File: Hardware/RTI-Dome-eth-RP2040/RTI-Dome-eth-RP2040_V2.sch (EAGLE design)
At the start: 104 parts, among them IC2 24LC128T-I_SN, IC3 FT232RL, IC4 RASPBERRY_PI_PICO, IC8 REG1117-3.3V, IC9 REG1117-5V, J2 XT60PW-M, U1 W5500, X13 PN61729-S, X9 J1011F21PNL

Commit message: Added transistor for stepper controller output
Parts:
- added R12, R22, R41: 1K, rcl:R-EU_R0805
- added T1, T2, T3: (no value), transistor:MMBT3904LT1-NPN-SOT23-BEC
- IC2: value 24LC128T-I_SN -> 24LC64T-I/SN; device rti:24LC128T-I_SN -> Microchip_By_element14_Batch_1:24LC64T-I/SN
- R13, R14, R19: value 1K -> 10K
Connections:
- removed net AT_PARK_PIN_LOOP: U$1G$1.A3
- removed net AT_PARK_PIN_LOOP_EXT: U$1G$1.Y3
- new net DIR-5V_PULLUP: R13.1, R22.1, T2.B
- new net DIR_5V_OUT: T2.E, X10-2.KL
- new net EN-5V_PULLUP: R12.1, R14.2, T1.B
- new net EN_5V_OUT: T1.E, X2-2.KL
- new net STEP-5V_PULLUP: R19.2, R41.1, T3.B
- new net STEP_5V_OUT: T3.E, X6-2.KL
- net BUTTON_EAST_OPEN-IN_EXT: no longer R44.2
- net BUTTON_WEST_CLOSE-IN_EXT: no longer R47.2
- net GND: now also U$1G$1.A3
- net HOME_SHUTTER_CLOSED-IN_EXT: no longer R50.2
- net M_DIR_5V: now also R22.2; no longer R19.2, X10-2.KL
- net M_EN_5V: now also R12.2; no longer R14.2, X2-2.KL
- net M_STEP_5V: now also R41.2; no longer R13.1, X6-2.KL
- net RG-11-IN_EXT: no longer R5.2
- net SHUTTER_OPENED-IN_EXT: no longer R48.2
- net VCC: now also T1.C, T2.C
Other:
- moved on the sheet: C23, C24, C27, C28, C4, C40, C41, C42, C43, C45, C5, C6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

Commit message: Fix some issue after the schematics snap to grid.
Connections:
- net BUTTON_EAST_OPEN-IN_EXT: now also R44.2
- net BUTTON_WEST_CLOSE-IN_EXT: now also R47.2
- net HOME_SHUTTER_CLOSED-IN_EXT: now also R50.2
- net RG-11-IN_EXT: now also R5.2
- net SHUTTER_OPENED-IN_EXT: now also R48.2
- net VCC: now also T3.C
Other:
- moved on the sheet: C1, C40, C41, C42, C43, C44, C45, C46, C8, IC3, IC4, R11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

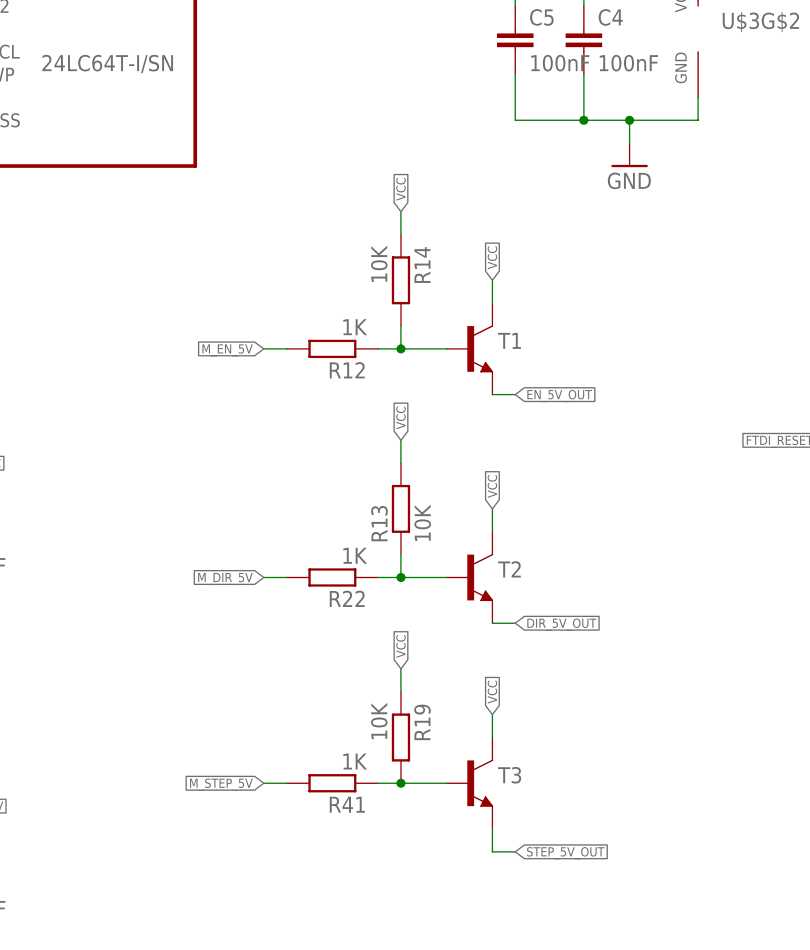
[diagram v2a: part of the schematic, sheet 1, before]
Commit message: Remove unused pull-up
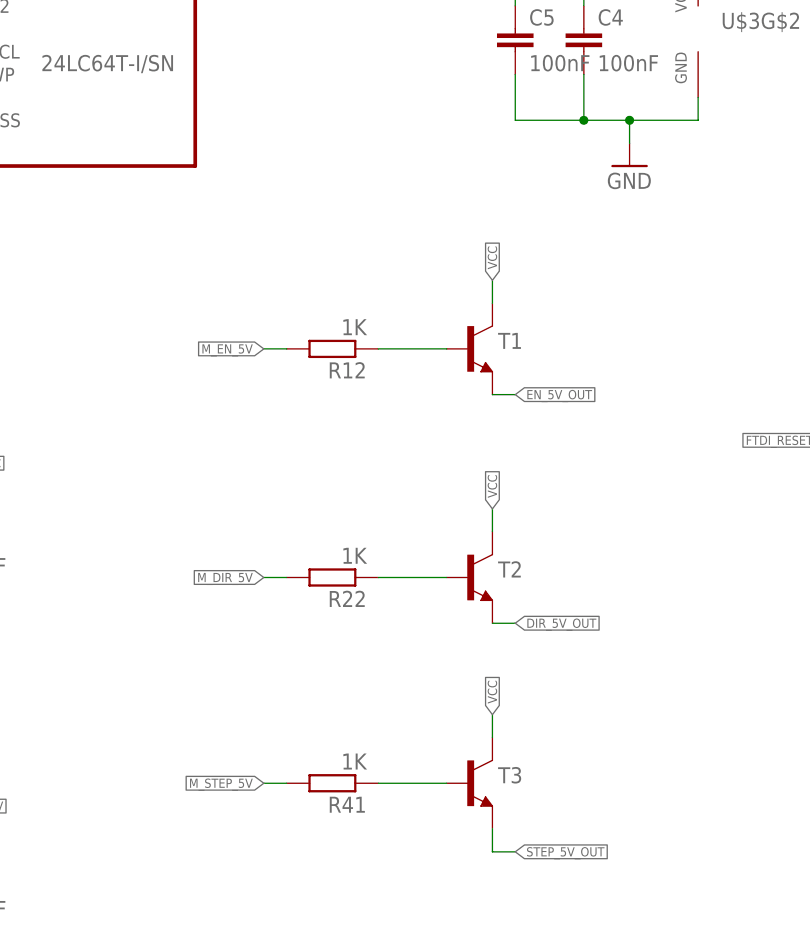
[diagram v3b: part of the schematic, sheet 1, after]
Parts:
- removed R13, R14, R19: 10K, rcl:R-EU_R0805
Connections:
- removed net DIR-5V_PULLUP: R13.1, R22.1, T2.B
- removed net EN-5V_PULLUP: R12.1, R14.2, T1.B
- removed net STEP-5V_PULLUP: R19.2, R41.1, T3.B
- new net DIR-5V_TR: R22.1, T2.B
- new net EN-5V_TR: R12.1, T1.B
- new net STEP-5V_TR: R41.1, T3.B
- net VCC: no longer R13.2, R14.1, R19.1
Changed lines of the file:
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@@
 <part name="GND4" library="supply1" library_urn="urn:adsk.eagle:library:371" deviceset="GND" device=""/>
 <part name="P+4" library="supply1" library_urn="urn:adsk.eagle:library:371" deviceset="VCC" device=""/>
-<part name="R13" library="rcl" library_urn="urn:adsk.eagle:library:334" deviceset="R-EU_" device="R0805" package3d_urn="urn:adsk.eagle:package:23553/2" value="10K">
+<part name="R15" library="rcl" library_urn="urn:adsk.eagle:library:334" deviceset="R-EU_" device="R0805" package3d_urn="urn:adsk.eagle:package:23553/2" value="4.7K">
 <spice>
 <pinmapping spiceprefix="R">
@@
 <attribute name="MPN" value="RT0805FRE074K7L"/>
 </part>
-<part name="R14" library="rcl" library_urn="urn:adsk.eagle:library:334" deviceset="R-EU_" device="R0805" package3d_urn="urn:adsk.eagle:package:23553/2" value="10K">
+<part name="R16" library="rcl" library_urn="urn:adsk.eagle:library:334" deviceset="R-EU_" device="R0805" package3d_urn="urn:adsk.eagle:package:23553/2" value="4.7K">
 <spice>
 <pinmapping spiceprefix="R">
@@
 <attribute name="MPN" value="RT0805FRE074K7L"/>
 </part>
-<part name="R15" library="rcl" library_urn="urn:adsk.eagle:library:334" deviceset="R-EU_" device="R0805" package3d_urn="urn:adsk.eagle:package:23553/2" value="4.7K">
+<part name="R17" library="rcl" library_urn="urn:adsk.eagle:library:334" deviceset="R-EU_" device="R0805" package3d_urn="urn:adsk.eagle:package:23553/2" value="4.7K">
 <spice>
 <pinmapping spiceprefix="R">
@@
 <attribute name="MPN" value="RT0805FRE074K7L"/>
 </part>
-<part name="R16" library="rcl" library_urn="urn:adsk.eagle:library:334" deviceset="R-EU_" device="R0805" package3d_urn="urn:adsk.eagle:package:23553/2" value="4.7K">
-<spice>
-<pinmapping spiceprefix="R">
-<pinmap gate="G$1" pin="1" pinorder="1"/>
-<pinmap gate="G$1" pin="2" pinorder="2"/>
-</pinmapping>
-</spice>
-<attribute name="MPN" value="RT0805FRE074K7L"/>
-</part>
-<part name="R17" library="rcl" library_urn="urn:adsk.eagle:library:334" deviceset="R-EU_" device="R0805" package3d_urn="urn:adsk.eagle:package:23553/2" value="4.7K">
-<spice>
-<pinmapping spiceprefix="R">
-<pinmap gate="G$1" pin="1" pinorder="1"/>
-<pinmap gate="G$1" pin="2" pinorder="2"/>
-</pinmapping>
-</spice>
-<attribute name="MPN" value="RT0805FRE074K7L"/>
-</part>
 <part name="R18" library="rcl" library_urn="urn:adsk.eagle:library:334" deviceset="R-EU_" device="R0805" package3d_urn="urn:adsk.eagle:package:23553/2" value="4.7K">
-<spice>
-<pinmapping spiceprefix="R">
-<pinmap gate="G$1" pin="1" pinorder="1"/>
-<pinmap gate="G$1" pin="2" pinorder="2"/>
-</pinmapping>
-</spice>
-<attribute name="MPN" value="RT0805FRE074K7L"/>
-</part>
-<part name="R19" library="rcl" library_urn="urn:adsk.eagle:library:334" deviceset="R-EU_" device="R0805" package3d_urn="urn:adsk.eagle:package:23553/2" value="10K">
 <spice>
 <pinmapping spiceprefix="R">
@@
 <attribute name="VALUE" x="306.07" y="254" size="1.778" layer="96" rot="R90"/>
 </instance>
-<instance part="R13" gate="G$1" x="96.52" y="147.32" smashed="yes" rot="R90">
-<attribute name="MPN" x="96.52" y="147.32" size="1.778" layer="96" rot="R90" display="off"/>
-<attribute name="NAME" x="95.0214" y="143.51" size="1.778" layer="95" rot="R90"/>
-<attribute name="VALUE" x="99.822" y="143.51" size="1.778" layer="96" rot="R90"/>
-</instance>
-<instance part="R14" gate="G$1" x="96.52" y="172.72" smashed="yes" rot="R270">
-<attribute name="MPN" x="96.52" y="172.72" size="1.778" layer="96" rot="R270" display="off"/>
-<attribute name="NAME" x="98.0186" y="176.53" size="1.778" layer="95" rot="R270"/>
-<attribute name="VALUE" x="93.218" y="176.53" size="1.778" layer="96" rot="R270"/>
-</instance>
 <instance part="R15" gate="G$1" x="313.69" y="241.3" smashed="yes" rot="R270">
 <attribute name="MPN" x="313.69" y="241.3" size="1.778" layer="96" rot="R270" display="off"/>
@@
 <attribute name="NAME" x="299.9486" y="245.11" size="1.778" layer="95" rot="R270"/>
 <attribute name="VALUE" x="295.148" y="245.11" size="1.778" layer="96" rot="R270"/>
-</instance>
-<instance part="R19" gate="G$1" x="96.52" y="121.92" smashed="yes" rot="R270">
-<attribute name="MPN" x="96.52" y="121.92" size="1.778" layer="96" rot="R270" display="off"/>
-<attribute name="NAME" x="98.0186" y="125.73" size="1.778" layer="95" rot="R270"/>
-<attribute name="VALUE" x="93.218" y="125.73" size="1.778" layer="96" rot="R270"/>
 </instance>
 <instance part="R6" gate="G$1" x="7.62" y="195.58" smashed="yes" rot="R90">
@@
 </segment>
 <segment>
-<pinref part="R14" gate="G$1" pin="1"/>
-<wire x1="96.52" y1="180.34" x2="96.52" y2="177.8" width="0.1524" layer="91"/>
-<label x="96.52" y="180.34" size="1.016" layer="95" rot="R90" xref="yes"/>
-</segment>
-<segment>
-<pinref part="R19" gate="G$1" pin="1"/>
-<wire x1="96.52" y1="129.54" x2="96.52" y2="127" width="0.1524" layer="91"/>
-<label x="96.52" y="129.54" size="1.016" layer="95" rot="R90" xref="yes"/>
-</segment>
-<segment>
-<pinref part="R13" gate="G$1" pin="2"/>
-<wire x1="96.52" y1="154.94" x2="96.52" y2="152.4" width="0.1524" layer="91"/>
-<label x="96.52" y="154.94" size="1.016" layer="95" rot="R90" xref="yes"/>
-</segment>
-<segment>
 <pinref part="T3" gate="G$1" pin="C"/>
 <wire x1="106.68" y1="124.46" x2="106.68" y2="121.92" width="0.1524" layer="91"/>
@@
 </segment>
 </net>
-<net name="DIR-5V_PULLUP" class="0">
+<net name="DIR-5V_TR" class="0">
 <segment>
 <pinref part="R22" gate="G$1" pin="1"/>
 <pinref part="T2" gate="G$1" pin="B"/>
-<wire x1="93.98" y1="139.7" x2="96.52" y2="139.7" width="0.1524" layer="91"/>
-<wire x1="96.52" y1="139.7" x2="101.6" y2="139.7" width="0.1524" layer="91"/>
-<wire x1="96.52" y1="139.7" x2="96.52" y2="142.24" width="0.1524" layer="91"/>
-<junction x="96.52" y="139.7"/>
-<pinref part="R13" gate="G$1" pin="1"/>
-</segment>
-</net>
-<net name="STEP-5V_PULLUP" class="0">
+<wire x1="93.98" y1="139.7" x2="101.6" y2="139.7" width="0.1524" layer="91"/>
+</segment>
+</net>
+<net name="STEP-5V_TR" class="0">
 <segment>
 <pinref part="R41" gate="G$1" pin="1"/>
 <pinref part="T3" gate="G$1" pin="B"/>
-<wire x1="93.98" y1="116.84" x2="96.52" y2="116.84" width="0.1524" layer="91"/>
-<wire x1="96.52" y1="116.84" x2="101.6" y2="116.84" width="0.1524" layer="91"/>
-<junction x="96.52" y="116.84"/>
-<pinref part="R19" gate="G$1" pin="2"/>
-</segment>
-</net>
-<net name="EN-5V_PULLUP" class="0">
+<wire x1="93.98" y1="116.84" x2="101.6" y2="116.84" width="0.1524" layer="91"/>
+</segment>
+</net>
+<net name="EN-5V_TR" class="0">
 <segment>
 <pinref part="R12" gate="G$1" pin="1"/>
 <pinref part="T1" gate="G$1" pin="B"/>
-<wire x1="93.98" y1="165.1" x2="96.52" y2="165.1" width="0.1524" layer="91"/>
-<wire x1="96.52" y1="165.1" x2="101.6" y2="165.1" width="0.1524" layer="91"/>
-<wire x1="96.52" y1="165.1" x2="96.52" y2="167.64" width="0.1524" layer="91"/>
-<junction x="96.52" y="165.1"/>
-<pinref part="R14" gate="G$1" pin="2"/>
-</segment>
-</net>
+<wire x1="93.98" y1="165.1" x2="101.6" y2="165.1" width="0.1524" layer="91"/>
+</segment>
+</net>

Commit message: New RP2040 shutter board
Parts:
- C1, C10, C11, C12, C13, C14, C15, C16, C17, C18, C19, C20, C21, C22, C23, C24, C27, C28, C3, C4, C40, C41, C42, C43, C44, C45, C46, C5, C6, C7, C8, C9: device rcl:C-EUC0805 -> rcl:C-EUC0603
- R1, R10, R11, R12, R15, R16, R17, R18, R2, R20, R21, R22, R23, R24, R25, R26, R27, R28, R29, R3, R30, R31, R32, R33, R34, R35, R36, R37, R38, R39, R4, R40, R41, R44, R45, R46, R47, R48, R49, R5, R50, R6, R7, R8, R9: device rcl:R-EU_R0805 -> rcl:R-EU_R0603

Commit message: Fix some components
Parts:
- removed U$2: MCP120T, MCP120T:MCP120T
- T1, T2, T3: value (none) -> MMBT3904LT1; device transistor:MMBT3904LT1-NPN-SOT23-BEC -> samacsys:MMBT3904LT1
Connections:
- net 3.3V: no longer U$2.VDD
- net GND: no longer U$2.VSS
- net RESET: no longer U$2.~RST
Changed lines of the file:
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@@
 <attribute name="MPN" value="RT0805FRE074K7L"/>
 </part>
-<part name="U$2" library="MCP120T" library_urn="urn:adsk.eagle:library:38117017" deviceset="MCP120T" device="" package3d_urn="urn:adsk.eagle:package:38117020/3">
-<attribute name="MPN" value="MCP120T-270I/TT"/>
-</part>
-<part name="GND18" library="supply1" library_urn="urn:adsk.eagle:library:371" deviceset="GND" device=""/>
 <part name="C13" library="rcl" library_urn="urn:adsk.eagle:library:334" deviceset="C-EU" device="C0603" package3d_urn="urn:adsk.eagle:package:23616/2" value="10nF">
 <spice>
@@
 <part name="U$1" library="rti" library_urn="urn:adsk.eagle:library:37256580" deviceset="74*541" device="B" package3d_urn="urn:adsk.eagle:package:37318379/2" value="74HCT541PWR"/>
 <part name="U$3" library="rti" library_urn="urn:adsk.eagle:library:37256580" deviceset="74*541" device="B" package3d_urn="urn:adsk.eagle:package:37318379/2" value="74LVC541APWR"/>
-<part name="T1" library="transistor" library_urn="urn:adsk.eagle:library:402" deviceset="*-NPN-" device="SOT23-BEC" package3d_urn="urn:adsk.eagle:package:28748/2" technology="MMBT3904LT1"/>
-<part name="T2" library="transistor" library_urn="urn:adsk.eagle:library:402" deviceset="*-NPN-" device="SOT23-BEC" package3d_urn="urn:adsk.eagle:package:28748/2" technology="MMBT3904LT1"/>
-<part name="T3" library="transistor" library_urn="urn:adsk.eagle:library:402" deviceset="*-NPN-" device="SOT23-BEC" package3d_urn="urn:adsk.eagle:package:28748/2" technology="MMBT3904LT1"/>
+<part name="T1" library="samacsys" library_urn="urn:adsk.eagle:library:37256869" deviceset="MMBT3904LT1" device="" package3d_urn="urn:adsk.eagle:package:28738/2"/>
+<part name="T2" library="samacsys" library_urn="urn:adsk.eagle:library:37256869" deviceset="MMBT3904LT1" device="" package3d_urn="urn:adsk.eagle:package:28738/2"/>
+<part name="T3" library="samacsys" library_urn="urn:adsk.eagle:library:37256869" deviceset="MMBT3904LT1" device="" package3d_urn="urn:adsk.eagle:package:28738/2"/>
 <part name="R12" library="rcl" library_urn="urn:adsk.eagle:library:334" deviceset="R-EU_" device="R0603" package3d_urn="urn:adsk.eagle:package:23555/3" value="1K">
 <spice>
@@
 <instance part="GND7" gate="1" x="187.96" y="226.06" smashed="yes">
 <attribute name="VALUE" x="185.42" y="223.52" size="1.778" layer="96"/>
-</instance>
-<instance part="U$2" gate="G$1" x="29.21" y="76.2" smashed="yes">
-<attribute name="MPN" x="29.21" y="76.2" size="1.778" layer="96" display="off"/>
-<attribute name="NAME" x="26.67" y="81.28" size="1.778" layer="95" align="center-left"/>
-<attribute name="VALUE" x="26.67" y="68.58" size="1.778" layer="96" align="center-left"/>
-</instance>
-<instance part="GND18" gate="1" x="13.97" y="68.58" smashed="yes">
-<attribute name="VALUE" x="11.43" y="66.04" size="1.778" layer="96"/>
 </instance>
 <instance part="GND16" gate="1" x="116.84" y="223.52" smashed="yes">
@@
 </segment>
 <segment>
-<pinref part="U$2" gate="G$1" pin="VSS"/>
-<wire x1="16.51" y1="73.66" x2="13.97" y2="73.66" width="0.1524" layer="91"/>
-<wire x1="13.97" y1="73.66" x2="13.97" y2="71.12" width="0.1524" layer="91"/>
-<pinref part="GND18" gate="1" pin="GND"/>
-</segment>
-<segment>
 <wire x1="119.38" y1="228.6" x2="116.84" y2="228.6" width="0.1524" layer="91"/>
 <wire x1="116.84" y1="228.6" x2="116.84" y2="226.06" width="0.1524" layer="91"/>
@@
 <wire x1="33.02" y1="213.36" x2="33.02" y2="210.82" width="0.1524" layer="91"/>
 <label x="33.02" y="213.36" size="1.016" layer="95" rot="R90" xref="yes"/>
-</segment>
-<segment>
-<pinref part="U$2" gate="G$1" pin="VDD"/>
-<wire x1="16.51" y1="76.2" x2="13.97" y2="76.2" width="0.1524" layer="91"/>
-<wire x1="13.97" y1="76.2" x2="13.97" y2="81.28" width="0.1524" layer="91"/>
-<label x="13.97" y="81.28" size="1.016" layer="95" rot="R90" xref="yes"/>
 </segment>
 <segment>
@@
 <net name="RESET" class="0">
 <segment>
-<pinref part="U$2" gate="G$1" pin="~RST"/>
-<label x="46.99" y="76.2" size="1.016" layer="95" xref="yes"/>
-<wire x1="46.99" y1="76.2" x2="44.45" y2="76.2" width="0.1524" layer="91"/>
-</segment>
-<segment>
 <pinref part="IC4" gate="G$1" pin="RUN"/>
